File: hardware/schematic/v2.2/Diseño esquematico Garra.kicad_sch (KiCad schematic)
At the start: 19 parts

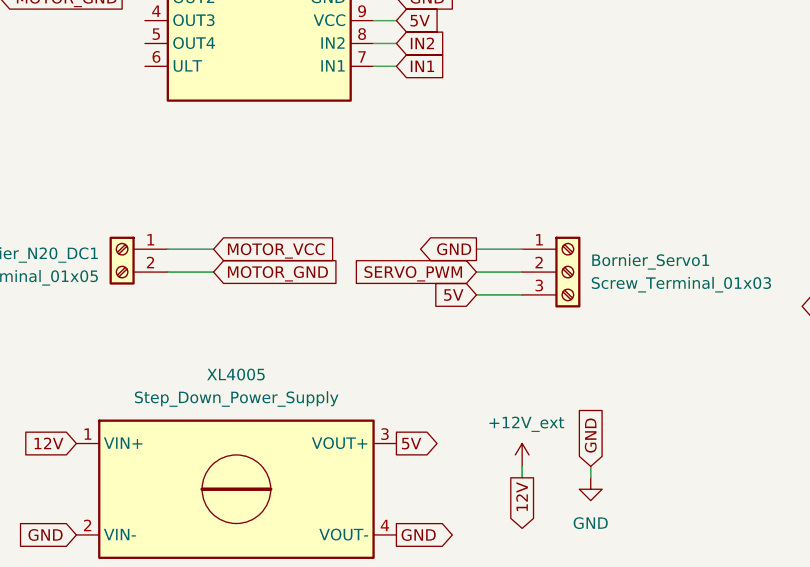
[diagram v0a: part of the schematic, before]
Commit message: feat: Update PCB structure
* refactor

* feat: PCB routing first stage completed

* docs: Schematics PDF added

* fix: PCB border colision

* feat: Copper layers added to the PCB

* feat: New PCB design with new components [LED, B_M]

* feat: add through holes for connectivity & GNDs links

* feat: hole diameter adjustment

* fix: PDF

* feat: change route system in PCB

* feat: add new esp32 schematic

* feat: complete PCB

* feat: take png and pdf from finished schematic

* feat: valid pdf PCB template

* fix: Expand PCB routes and copper holes

* feat: Change PCB design and clearance

---------

Co-authored-by: ManuSavenia <saveniamanuel@egmail.com>
Co-authored-by: Iván Valentín Polanis <polanis.ivan@alu.ing.unlp.edu.ar>
Co-authored-by: Gonzalo Blasco <gonzagabino@gmail.com>
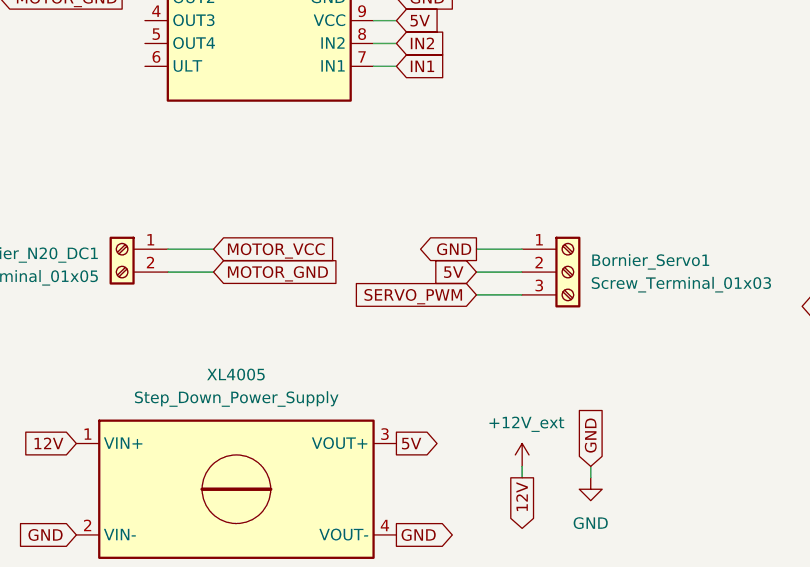
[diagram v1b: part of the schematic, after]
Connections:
- net 5V: now also Bornier_Servo1.2 (Pin_2); no longer Bornier_Servo1.3 (Pin_3)
- net SERVO_PWM: now also Bornier_Servo1.3 (Pin_3); no longer Bornier_Servo1.2 (Pin_2)
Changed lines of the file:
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@@
 		)
 	)
-	(global_label "SERVO_PWM"
+	(global_label "5V"
 		(shape input)
 		(at 184.15 63.5 180)
@@
 		)
 	)
-	(global_label "5V"
+	(global_label "SERVO_PWM"
 		(shape input)
 		(at 184.15 66.04 180)

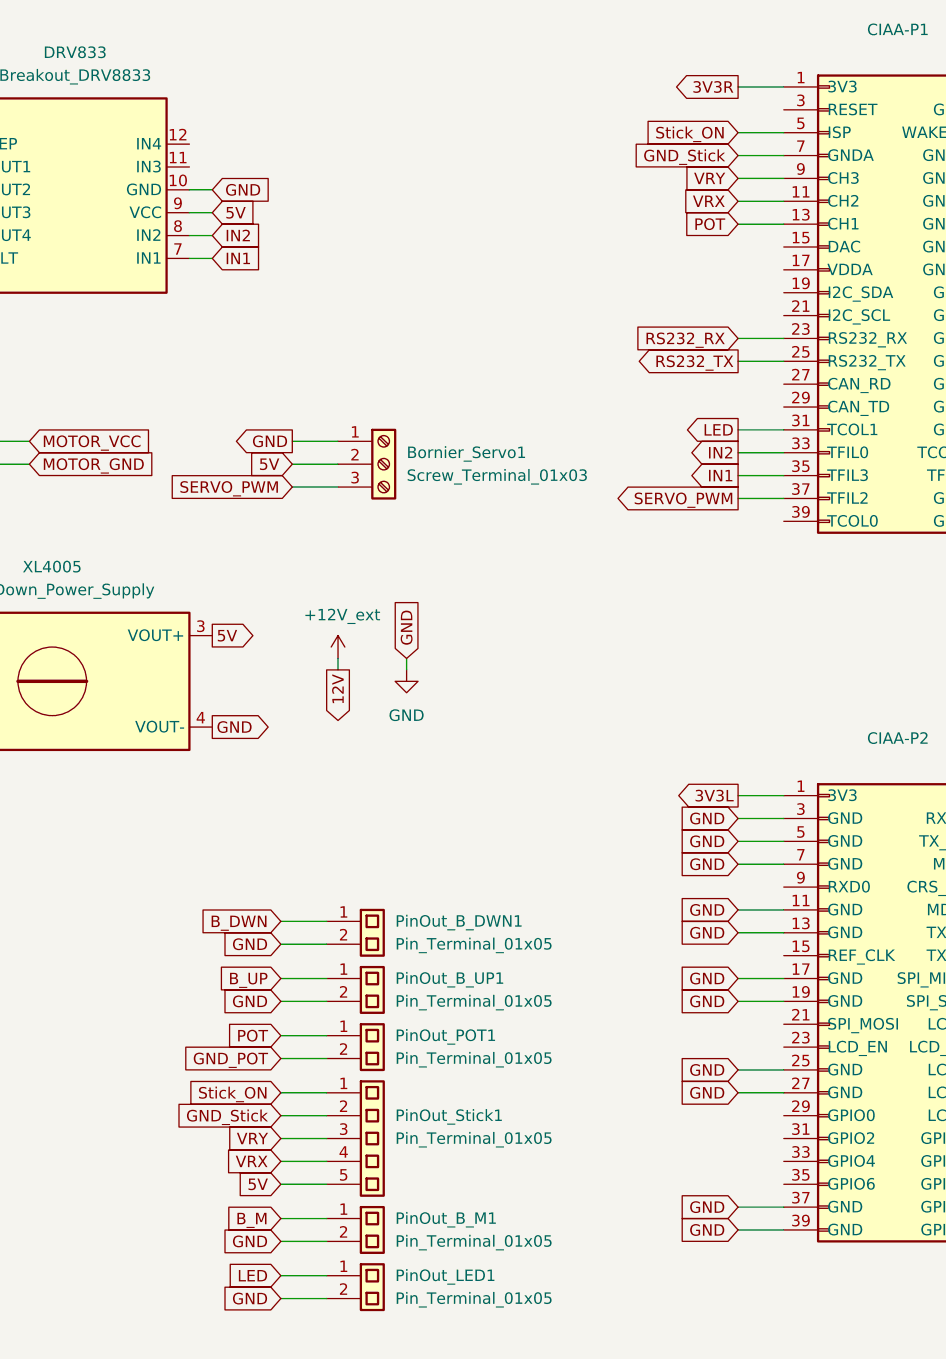
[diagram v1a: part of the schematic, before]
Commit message: feat: Change Stick_on from ISP to CAN_RD
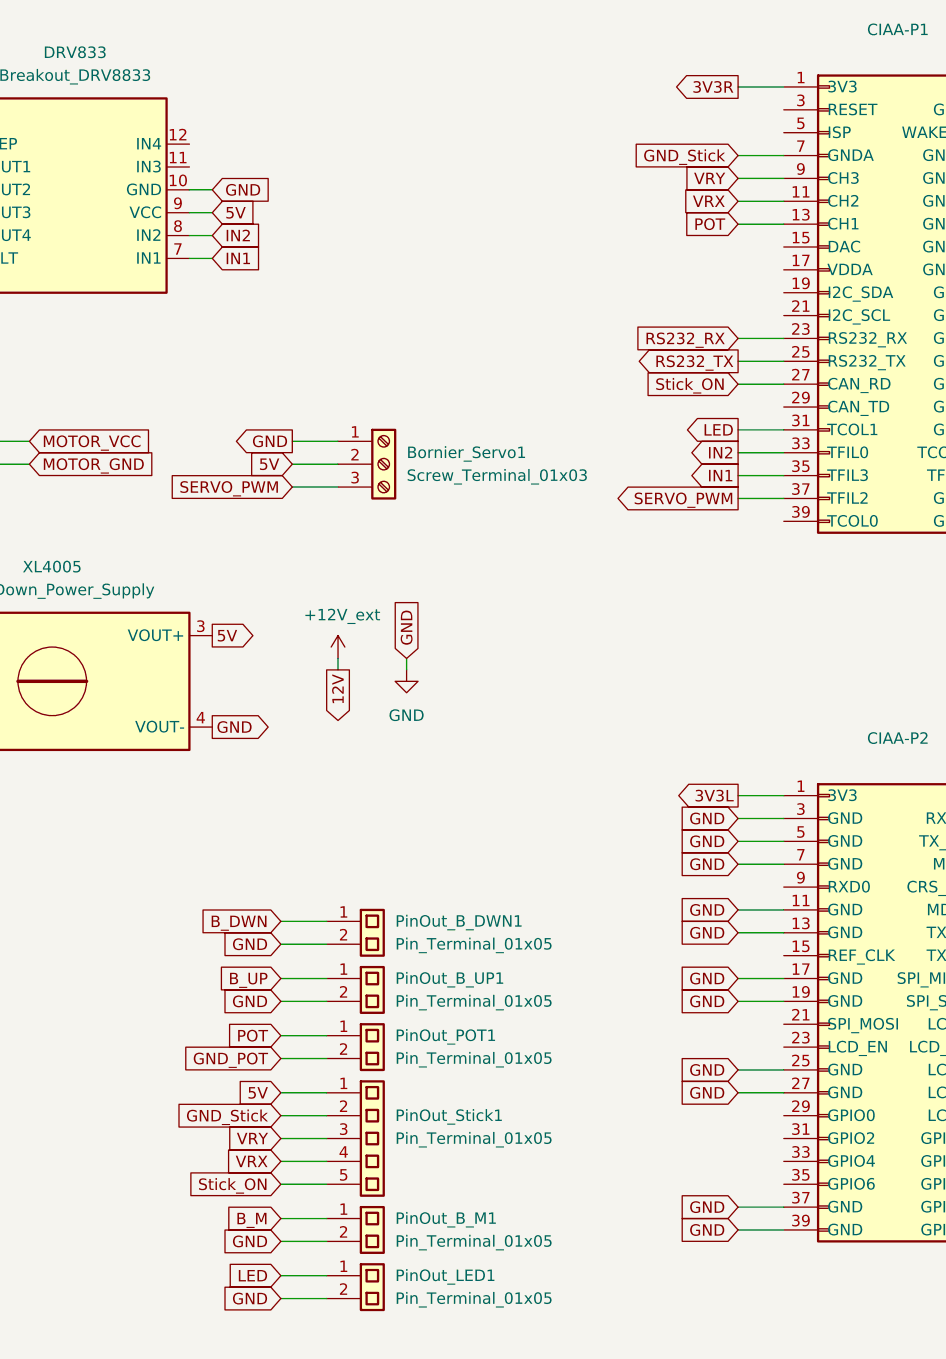
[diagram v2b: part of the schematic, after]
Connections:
- net 5V: now also PinOut_Stick1.1 (Pin_1); no longer PinOut_Stick1.5 (Pin_5)
- net Stick_ON: now also CIAA-P1.27 (CAN_RD), PinOut_Stick1.5 (Pin_5); no longer CIAA-P1.5 (ISP), PinOut_Stick1.1 (Pin_1)
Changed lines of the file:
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@@
-	(wire
-		(pts
-			(xy 233.68 26.67) (xy 238.76 26.67)
-		)
-		(stroke
-			(width 0)
-			(type default)
-		)
-	)
 	(wire
 		(pts
@@
 		(pts
 			(xy 233.68 100.33) (xy 238.76 100.33)
+		)
+		(stroke
+			(width 0)
+			(type default)
+		)
+	)
+	(wire
+		(pts
+			(xy 233.68 54.61) (xy 238.76 54.61)
 		)
 		(stroke
@@
 		)
 	)
-	(global_label "5V"
+	(global_label "Stick_ON"
 		(shape input)
 		(at 182.88 143.51 180)
@@
 		)
 	)
-	(global_label "Stick_ON"
+	(global_label "5V"
 		(shape input)
 		(at 182.88 133.35 180)
@@
 	(global_label "Stick_ON"
 		(shape input)
-		(at 233.68 26.67 180)
-		(effects
-			(font
-				(size 1.27 1.27)
-			)
-			(justify right)
-		)
-		(property "Intersheetrefs" "${INTERSHEET_REFS}"
-			(at 233.68 26.67 0)
-			(effects
-				(font
+		(at 233.68 54.61 180)
+		(effects
+			(font
+				(size 1.27 1.27)
+			)
+			(justify right)
+		)
+		(property "Intersheetrefs" "${INTERSHEET_REFS}"
+			(at 233.68 54.61 0)
+			(effects
+				(font
